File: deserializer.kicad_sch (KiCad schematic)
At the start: 44 parts

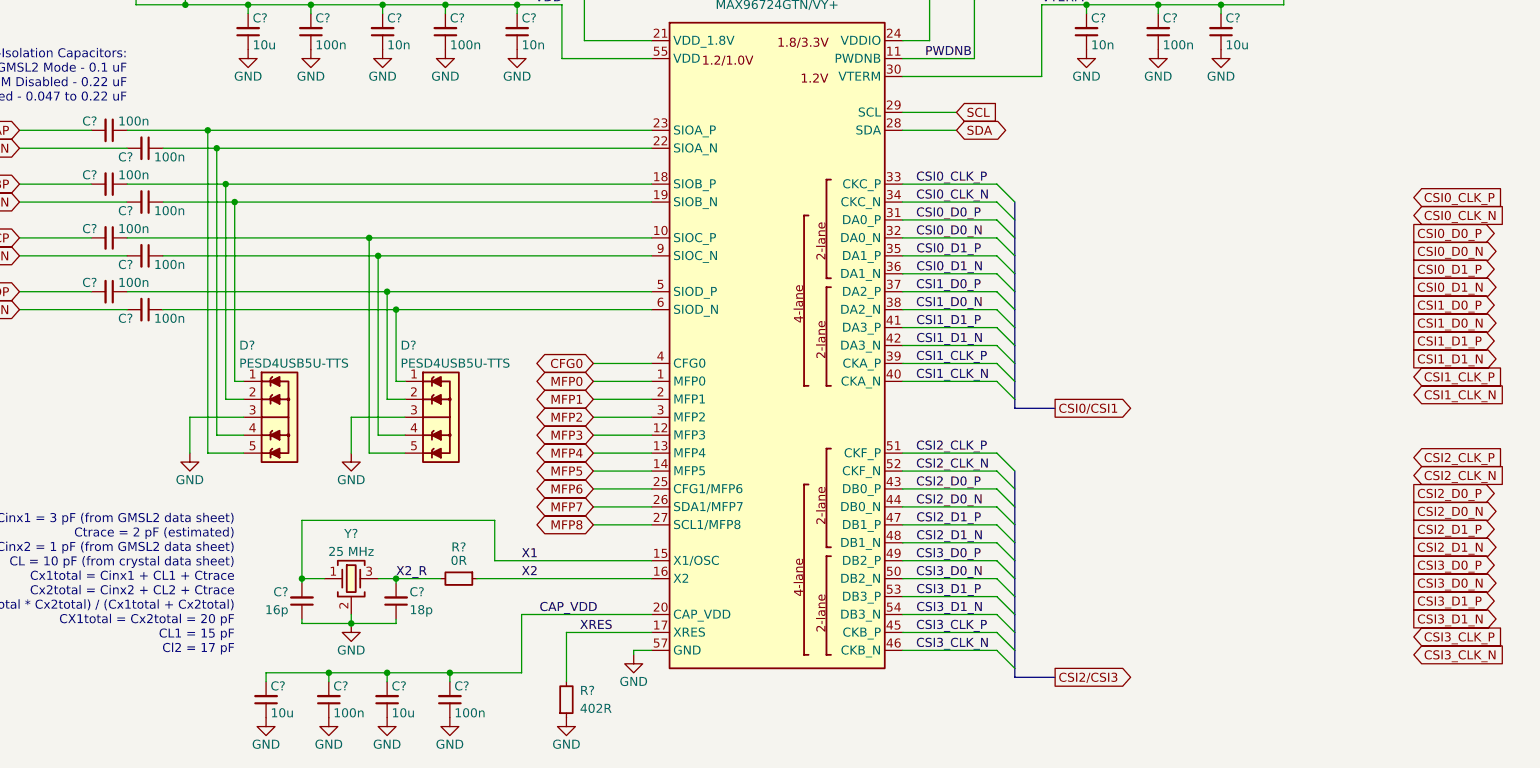
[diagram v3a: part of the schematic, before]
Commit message: [#51627] fix diagram, Deserializer: remove unused labels, change diodes symbol
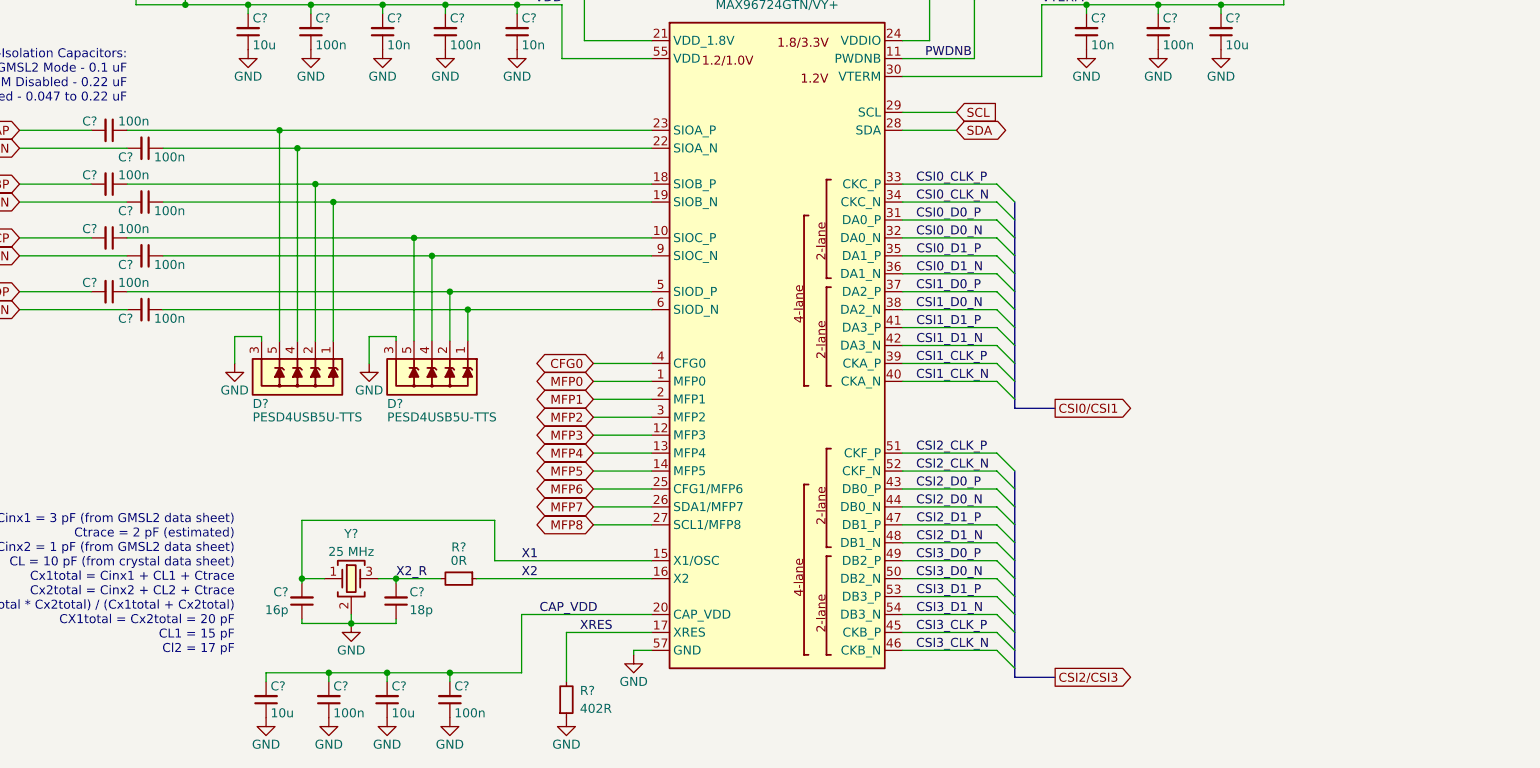
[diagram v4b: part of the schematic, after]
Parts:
- removed D?: PESD4USB5U-TTS, antmicro-footprints:DFN2510D-10, symbol antmicroTVSDiodes:PESD4USB5U-TTS
- added D?: PESD4USB5U-TTS, antmicro-footprints:DFN2510D-10, symbol antmicroTVSDiodes:PESD4USB5U-TTS
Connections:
- net GND: now also D?.3, D?.8
- net at C?.1, U?.18 (SIOB_P): now also D?.2
- net at C?.1, U?.19 (SIOB_N): now also D?.1
- net at C?.1, U?.22 (SIOA_N): now also D?.4
- net at C?.1, U?.23 (SIOA_P): now also D?.5

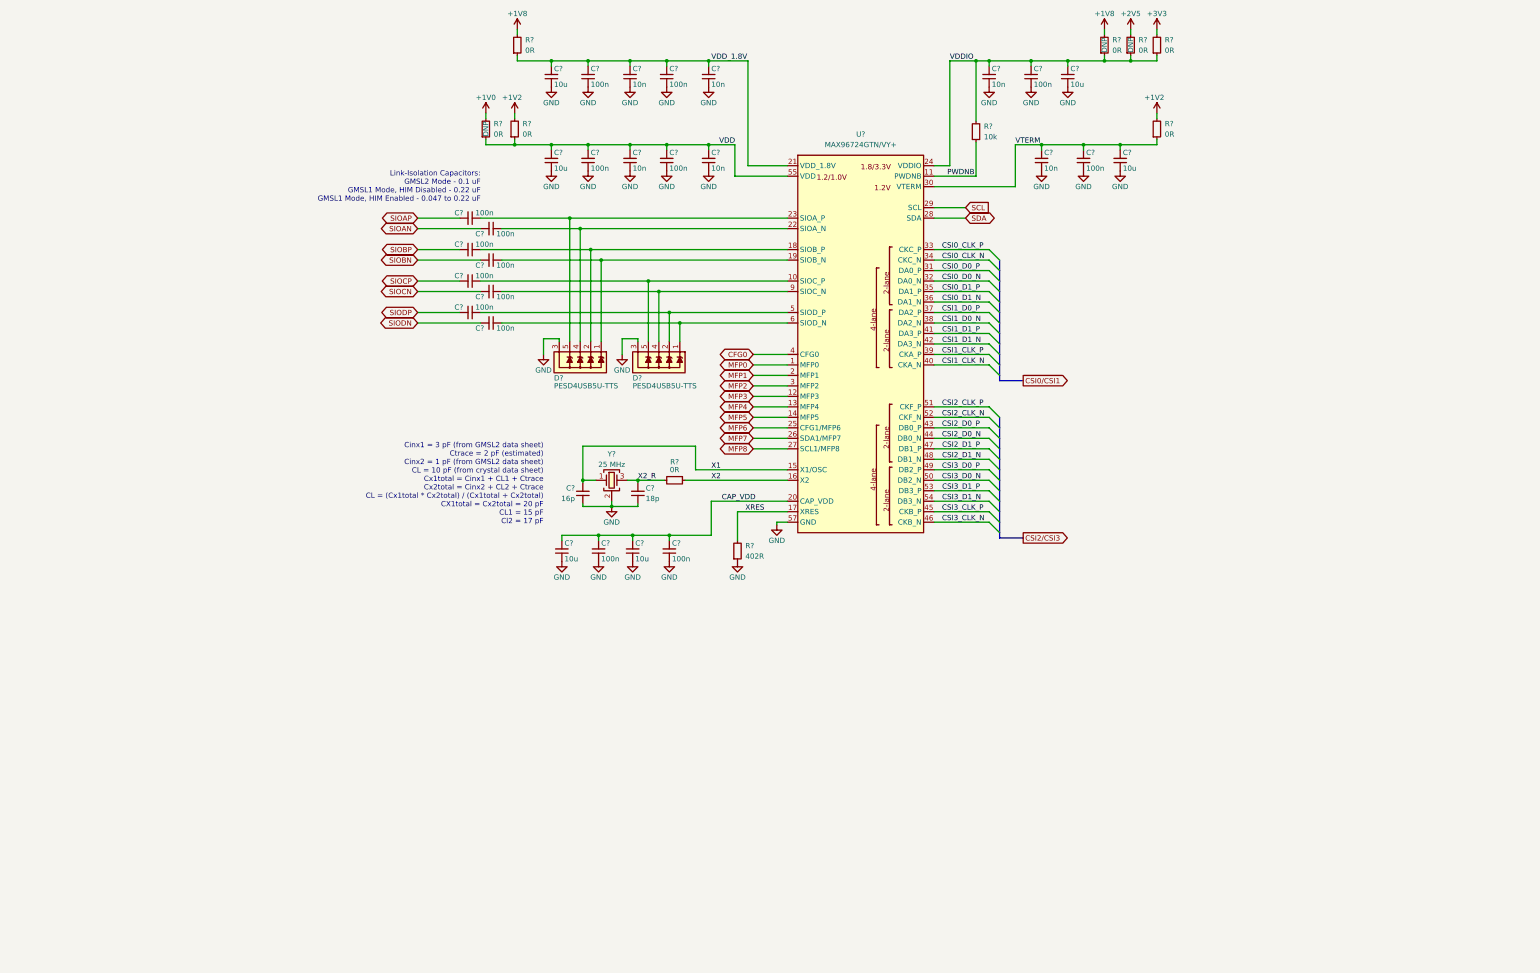
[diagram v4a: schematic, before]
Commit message: [#51627] Deserializer: move crystal, add config pins, add MFP to bus
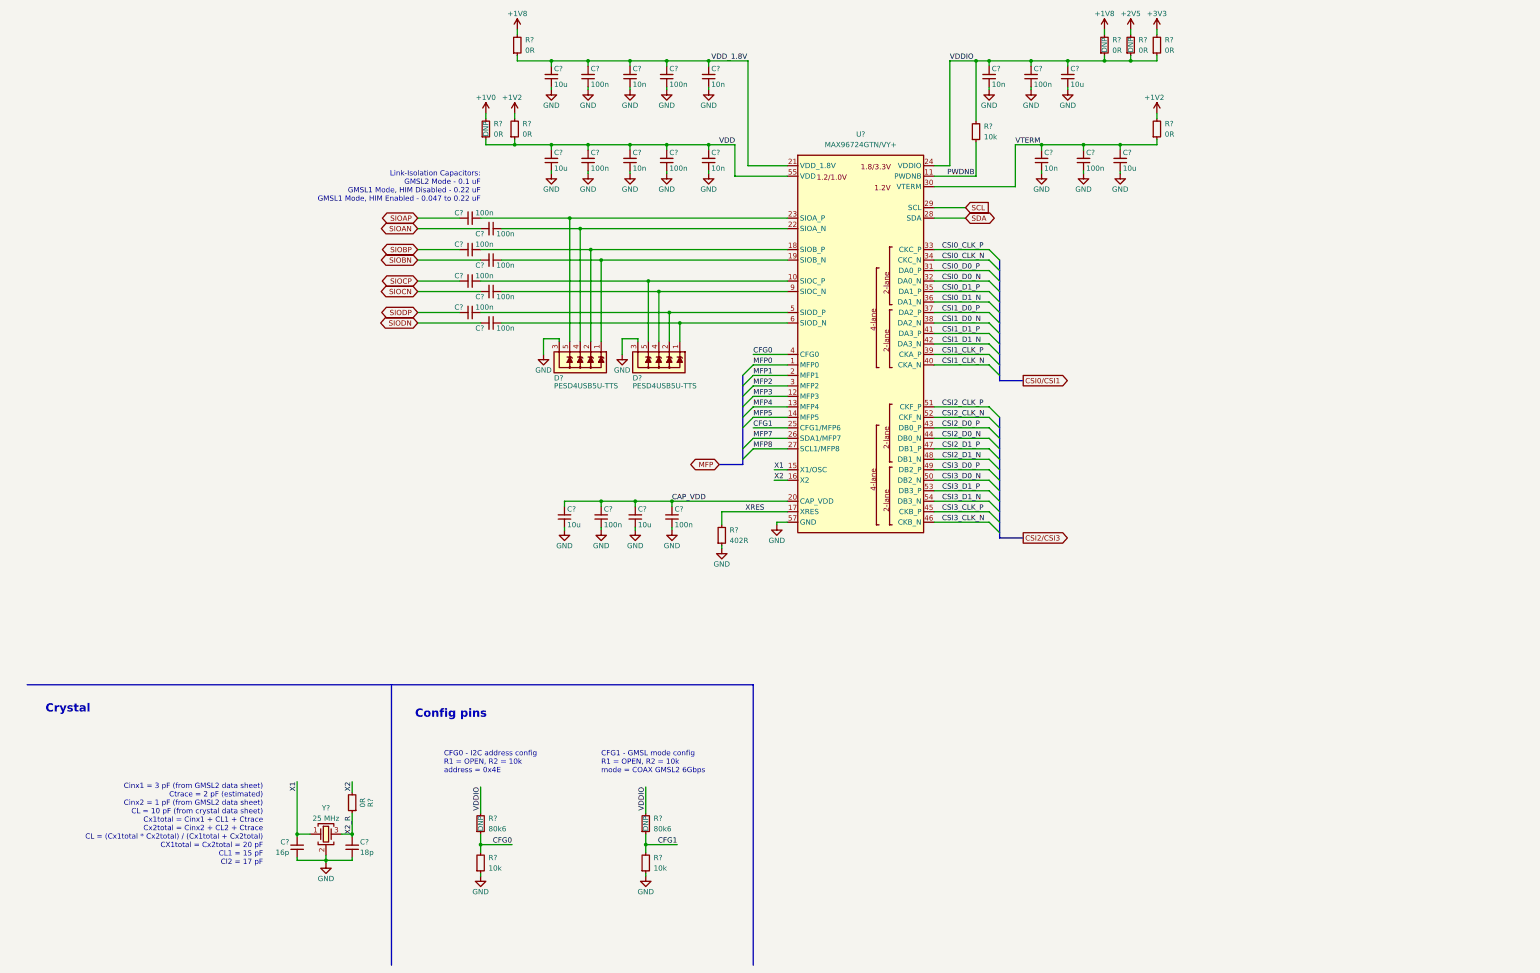
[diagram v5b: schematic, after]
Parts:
- removed C?: C_18p_0402, antmicro-footprints:C_0402_1005Metric, symbol antmicroCapacitors0402:C_18p_0402
- removed C?: C_16p_0402, antmicro-footprints:C_0402_1005Metric, symbol antmicroCapacitors0402:C_16p_0402
- removed R?: R_0R_0402, antmicro-footprints:R_0402_1005Metric, symbol antmicroResistors0402:R_0R_0402
- removed Y?: Resonator_25MHz_ABM8G, antmicro-footprints:Oscillator_SMD_Geyer_KX-7-4Pin_3.2x2.5mm, symbol antmicroResonators:Resonator_25MHz_ABM8G
- added C?: C_16p_0402, antmicro-footprints:C_0402_1005Metric, symbol antmicroCapacitors0402:C_16p_0402
- added C?: C_18p_0402, antmicro-footprints:C_0402_1005Metric, symbol antmicroCapacitors0402:C_18p_0402
- added R? (x2): R_10k_0402, antmicro-footprints:R_0402_1005Metric, symbol antmicroResistors0402:R_10k_0402
- added R?: R_0R_0402, antmicro-footprints:R_0402_1005Metric, symbol antmicroResistors0402:R_0R_0402
- added R? (x2): R_80k6_0402, antmicro-footprints:R_0402_1005Metric, symbol antmicroResistors0402:R_80k6_0402
- added Y?: Resonator_25MHz_ABM8G, antmicro-footprints:Oscillator_SMD_Geyer_KX-7-4Pin_3.2x2.5mm, symbol antmicroResonators:Resonator_25MHz_ABM8G
- D? (x2): footprint antmicro-footprints:DFN2510D-10 -> antmicro-footprints:DFN-10_2.5x1mm
- R?: Manufacturer Bourns -> Vishay
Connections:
- net CFG0: now also R?.1, R?.2
- net GND: now also C?.1, C?.1, R?.1, R?.1, Y?.2 (SH), Y?.4 (SH)
- net VDDIO: now also R?.2, R?.2
- net X1: now also C?.2, Y?.1
- net X2: now also R?.2
- net X2_R: now also C?.2, R?.1, Y?.3
- net MFP6 renamed CFG1
- net CFG1: now also R?.1, R?.2
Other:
- note added: "CFG0 - I2C address config R1 = OPEN, R2 = 10k address = 0x4E"
- note added: "CFG1 - GMSL mode config R1 = OPEN, R2 = 10k mode = COAX GMSL2 6Gbps"
- note added: "Config pins"
- note added: "Crystal"
- moved on the sheet: C?, R?

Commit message: [#51632] Power: add current limit, buck conv Connectors: add buffer gates, remove one FFC conn
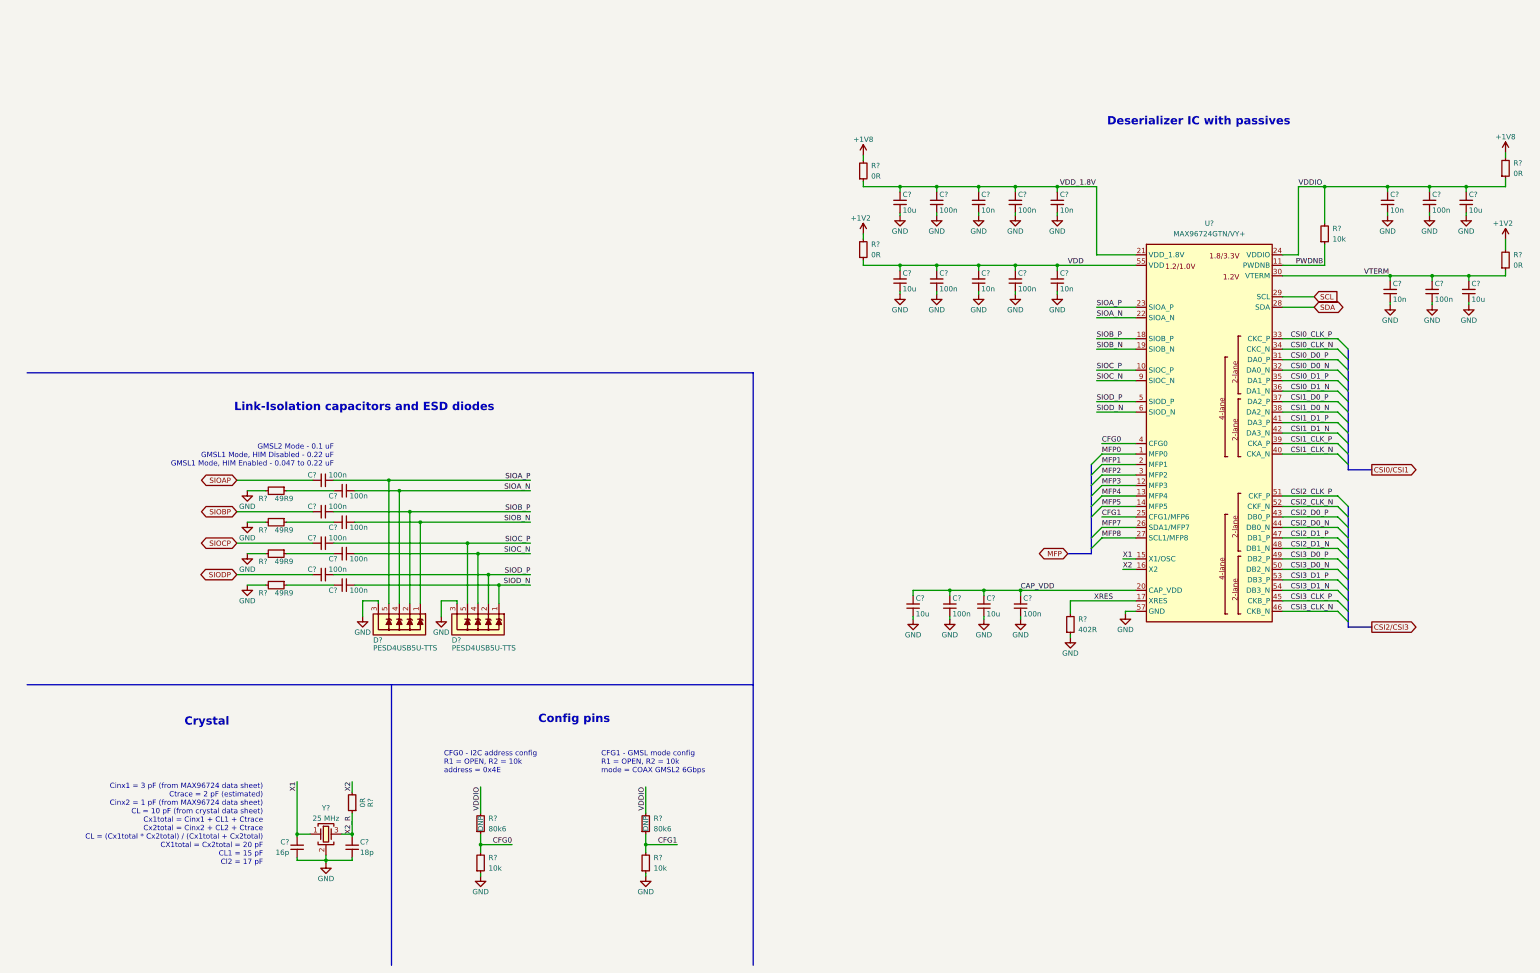
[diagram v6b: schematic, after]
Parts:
- removed C? (x8): C_100n_0402, antmicro-footprints:C_0402_1005Metric, symbol antmicroCapacitors0402:C_100n_0402
- removed D? (x2): PESD4USB5U-TTS, antmicro-footprints:DFN-10_2.5x1mm, symbol antmicroTVSDiodes:PESD4USB5U-TTS
- removed R? (x4): R_0R_0402, antmicro-footprints:R_0402_1005Metric, symbol antmicroResistors0402:R_0R_0402
- added C? (x8): C_100n_0402, antmicro-footprints:C_0402_1005Metric, symbol antmicroCapacitors0402:C_100n_0402
- added D? (x2): PESD4USB5U-TTS, antmicro-footprints:DFN-10_2.5x1mm, symbol antmicroTVSDiodes:PESD4USB5U-TTS
- added R? (x4): R_49R9_0402, antmicro-footprints:R_0402_1005Metric, symbol antmicroResistors0402:R_49R9_0402
- added R?: R_0R_0402, antmicro-footprints:R_0402_1005Metric, symbol antmicroResistors0402:R_0R_0402
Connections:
- net +1V8: now also R?.2
- net GND: now also D?.3, D?.3, D?.8, D?.8, R?.2, R?.2, R?.2, R?.2
- net SIOAP: now also C?.2
- net SIOBP: now also C?.2
- net SIOCP: now also C?.2
- net SIODP: now also C?.2
- net VDDIO: now also R?.1
- net SIOC_P: now reaches U?.10 (SIOC_P)
- net SIOC_P: now also C?.1, D?.5
- net SIOB_P: now reaches U?.18 (SIOB_P)
- net SIOB_P: now also C?.1, D?.2
- net SIOD_N: now reaches U?.6 (SIOD_N)
- net SIOD_N: now also C?.1, D?.1
- net SIOB_N: now reaches U?.19 (SIOB_N)
- net SIOB_N: now also C?.1, D?.1
- net SIOA_N: now reaches U?.22 (SIOA_N)
- net SIOA_N: now also C?.1, D?.4
- net SIOA_P: now reaches U?.23 (SIOA_P)
- net SIOA_P: now also C?.1, D?.5
- net SIOD_P: now reaches U?.5 (SIOD_P)
- net SIOD_P: now also C?.1, D?.2
- net SIOC_N: now reaches U?.9 (SIOC_N)
- net SIOC_N: now also C?.1, D?.4
- new net: C?.2, R?.1 (x4)
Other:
- note added: "Cinx1 = 3 pF (from MAX96724 data sheet) Ctrace = 2 pF (estimated) Cinx2 = 1 pF (from MAX96724 data sheet) CL = 10 pF (from crystal data sheet) Cx1total = Cinx1 + CL1 + Ctrace Cx2total = Cinx2 + CL2 + Ctrace CL = (Cx1total * Cx2total) / (Cx1total + Cx2total) CX1total = Cx2total = 20 pF CL1 = 15 pF Cl2 = 17 pF"
- note added: "Deserializer IC with passives"
- note added: "GMSL2 Mode - 0.1 uF GMSL1 Mode, HIM Disabled - 0.22 uF GMSL1 Mode, HIM Enabled - 0.047 to 0.22 uF"
- note added: "Link-Isolation capacitors and ESD diodes"
- note removed: "Cinx1 = 3 pF (from GMSL2 data sheet) Ctrace = 2 pF (estimated) Cinx2 = 1 pF (from GMSL2 data sheet) CL = 10 pF (from crystal data sheet) Cx1total = Cinx1 + CL1 + Ctrace Cx2total = Cinx2 + CL2 + Ctrace CL = (Cx1total * Cx2total) / (Cx1total + Cx2total) CX1total = Cx2total = 20 pF CL1 = 15 pF Cl2 = 17 pF"
- note removed: "Link-Isolation Capacitors: GMSL2 Mode - 0.1 uF GMSL1 Mode, HIM Disabled - 0.22 uF GMSL1 Mode, HIM Enabled - 0.047 to 0.22 uF"
- moved on the sheet: C?, R?, U?

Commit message: Schematics done
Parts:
- gave numbers to parts that had none: 49
